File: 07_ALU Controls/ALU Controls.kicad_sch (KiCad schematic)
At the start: 7 parts, among them J1 Operators 1, J2 Operators 2, J3 Operand, J4 Data Bus, J5 Alu-Out Bus, J6 Input 1, J7 Input 2

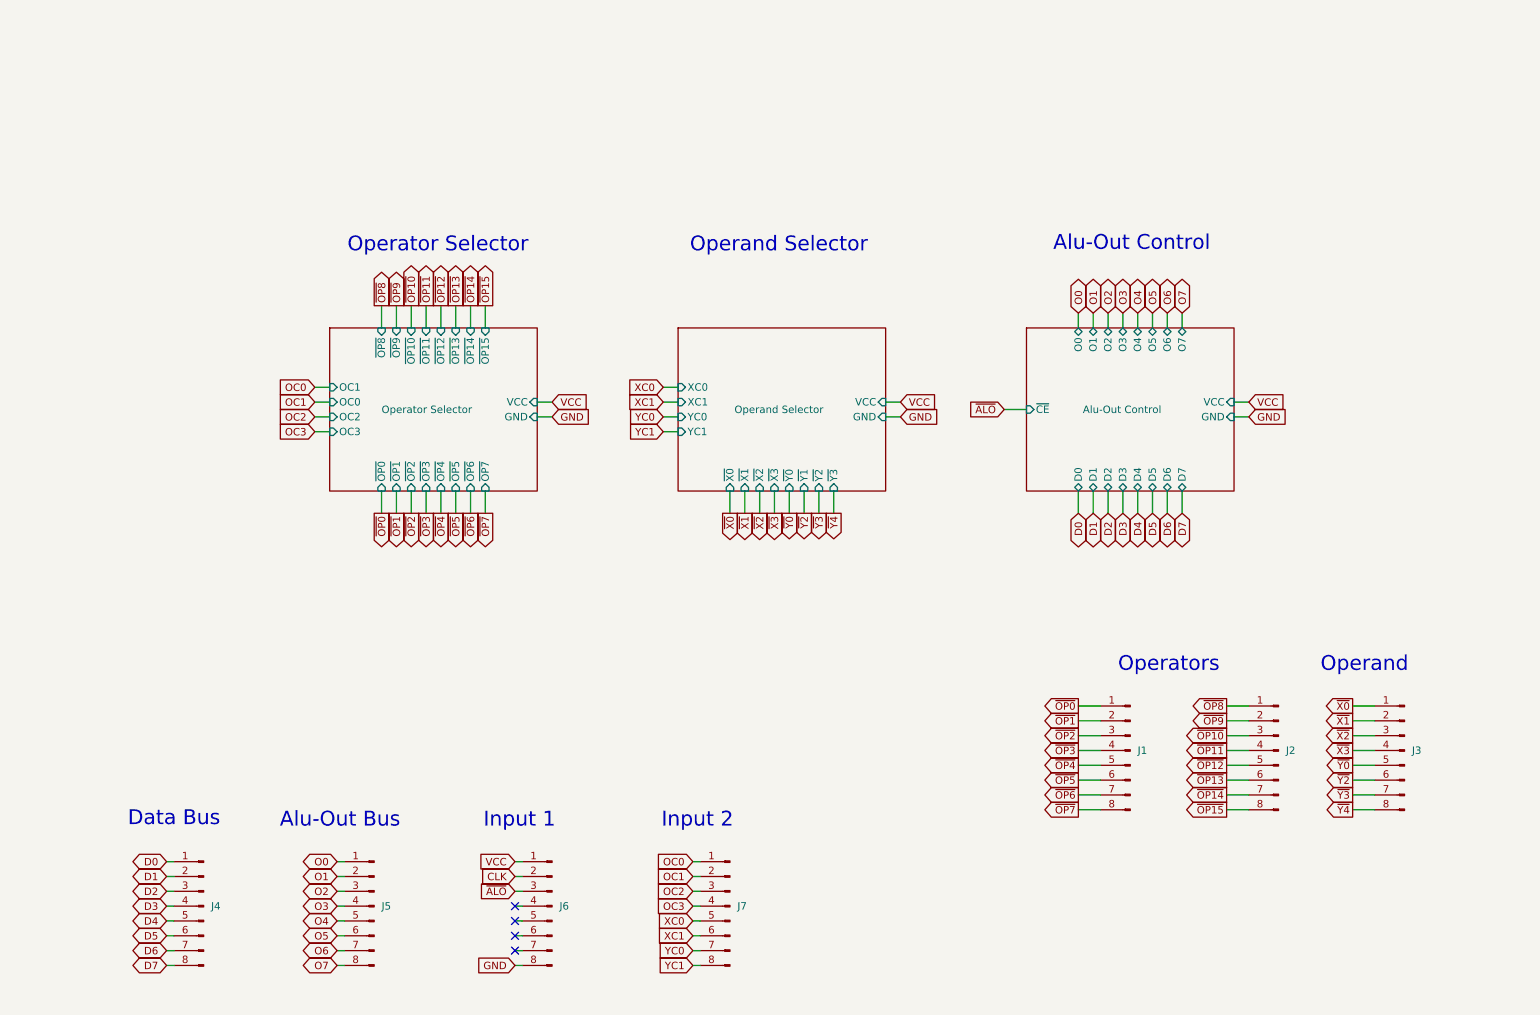
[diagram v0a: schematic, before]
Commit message: Last revision of the cpu, all boards have been ordered. Implementation to be tested and documented in following commits.
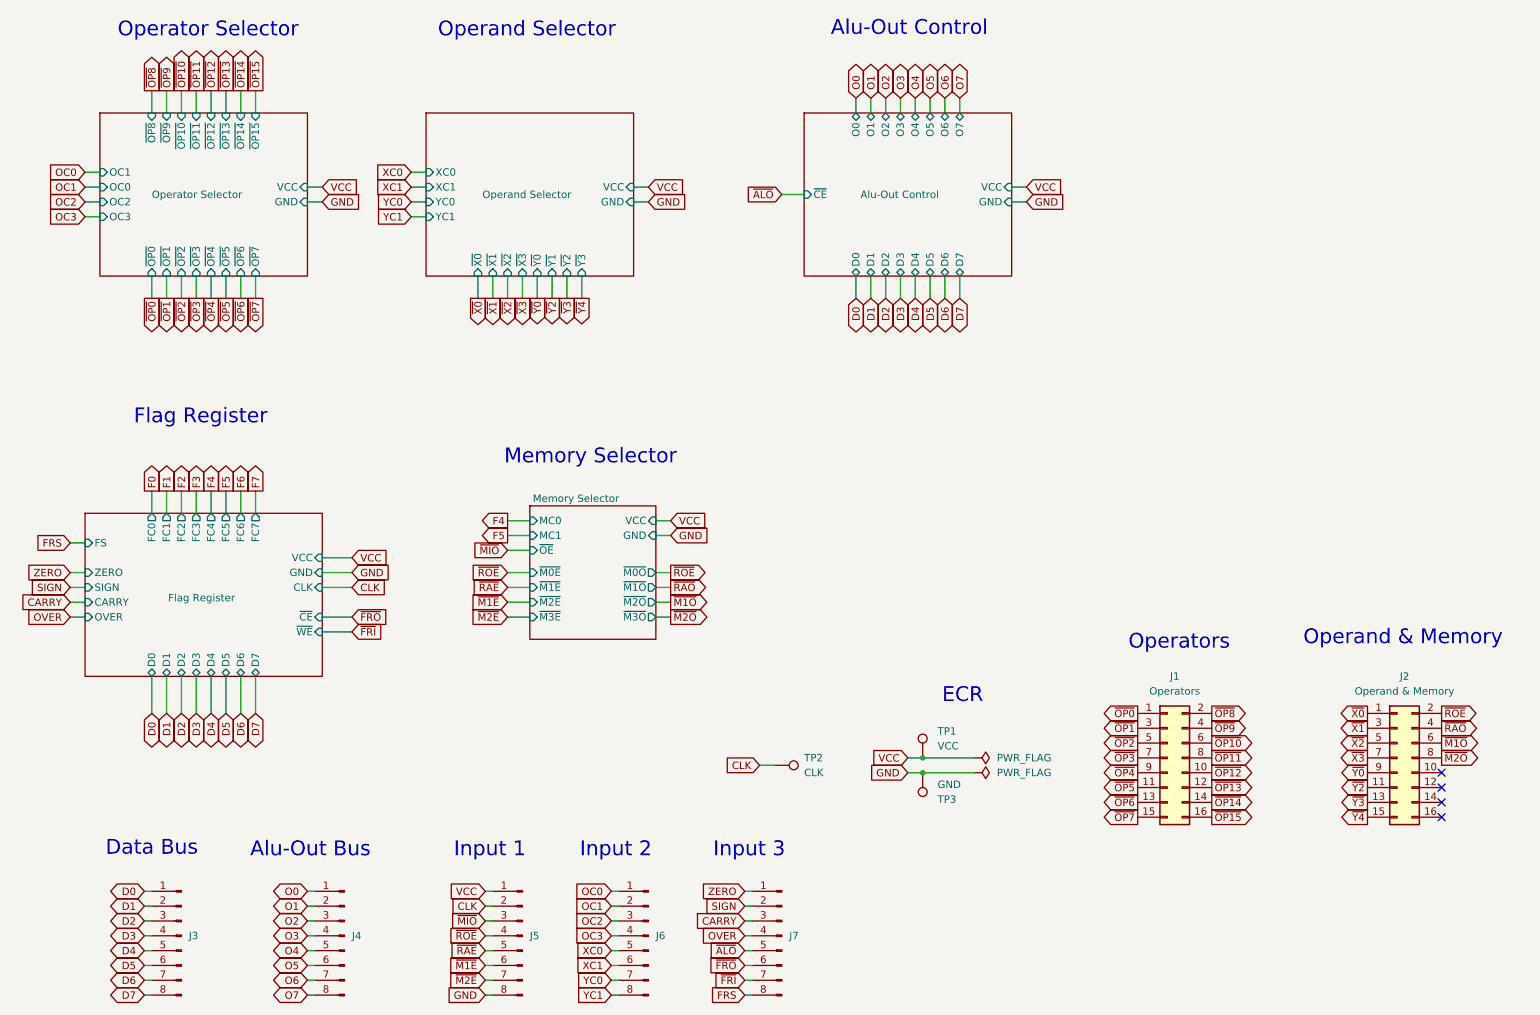
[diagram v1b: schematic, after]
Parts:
- removed J1: Operators 1, Custom:PinHeader_1x08_P2.54mm_Vertical, symbol Connector:Conn_01x08_Pin
- removed J2: Operators 2, Custom:PinHeader_1x08_P2.54mm_Vertical, symbol Connector:Conn_01x08_Pin
- removed J3: Operand, Custom:PinHeader_1x08_P2.54mm_Vertical, symbol Connector:Conn_01x08_Pin
- added J1: Operators, Connector_PinHeader_2.54mm:PinHeader_2x08_P2.54mm_Horizontal, symbol Connector_Generic:Conn_02x08_Odd_Even
- added J2: Operand & Memory, Connector_PinHeader_2.54mm:PinHeader_2x08_P2.54mm_Horizontal, symbol Connector_Generic:Conn_02x08_Odd_Even
- added J7: Input 3, Custom:PinHeader_1x08_P2.54mm_Horizontal, symbol Connector:Conn_01x08_Pin
- added TP1: VCC, TestPoint:TestPoint_Loop_D3.50mm_Drill0.9mm_Beaded, symbol Connector:TestPoint
- added TP2: CLK, TestPoint:TestPoint_Loop_D3.50mm_Drill0.9mm_Beaded, symbol Connector:TestPoint
- added TP3: GND, TestPoint:TestPoint_Loop_D3.50mm_Drill0.9mm_Beaded, symbol Connector:TestPoint
- renumbered J4 to J3, J5 to J4, J6 to J5, J7 to J6
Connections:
- net CLK: now also TP2.1
- net GND: now also TP3.1
- net VCC: now also TP1.1
- net ~{ALO}: now also J7.5 (Pin_5); no longer J5.3 (Pin_3)
- net ~{OP0}: now also J1.1 (Pin_1)
- net ~{OP10}: now also J1.6 (Pin_6)
- net ~{OP11}: now also J1.8 (Pin_8)
- net ~{OP12}: now also J1.10 (Pin_10)
- net ~{OP13}: now also J1.12 (Pin_12)
- net ~{OP14}: now also J1.14 (Pin_14)
- net ~{OP15}: now also J1.16 (Pin_16)
- net ~{OP1}: now also J1.3 (Pin_3)
- net ~{OP2}: now also J1.5 (Pin_5)
- net ~{OP3}: now also J1.7 (Pin_7)
- net ~{OP4}: now also J1.9 (Pin_9)
- net ~{OP5}: now also J1.11 (Pin_11)
- net ~{OP6}: now also J1.13 (Pin_13)
- net ~{OP7}: now also J1.15 (Pin_15)
- net ~{OP8}: now also J1.2 (Pin_2)
- net ~{OP9}: now also J1.4 (Pin_4)
- net ~{X0}: now also J2.1 (Pin_1)
- net ~{X1}: now also J2.3 (Pin_3)
- net ~{X2}: now also J2.5 (Pin_5)
- net ~{X3}: now also J2.7 (Pin_7)
- net ~{Y0}: now also J2.9 (Pin_9)
- net ~{Y2}: now also J2.11 (Pin_11)
- net ~{Y3}: now also J2.13 (Pin_13)
- net ~{Y4}: now also J2.15 (Pin_15)
- net ~{ROE}: now reaches J5.4 (Pin_4)
- net ~{ROE}: now also J2.2 (Pin_2)
- net ~{RAE}: now reaches J5.5 (Pin_5)
- net ~{M1E}: now reaches J5.6 (Pin_6)
- net ~{M2E}: now reaches J5.7 (Pin_7)
- new net CARRY: J7.3 (Pin_3)
- new net FRS: J7.8 (Pin_8)
- new net OVER: J7.4 (Pin_4)
- new net SIGN: J7.2 (Pin_2)
- new net ZERO: J7.1 (Pin_1)
- new net ~{FRI}: J7.7 (Pin_7)
- new net ~{FRO}: J7.6 (Pin_6)
- new net ~{M1O}: J2.6 (Pin_6)
- new net ~{M2O}: J2.8 (Pin_8)
- new net ~{MIO}: J5.3 (Pin_3)
- new net ~{RAO}: J2.4 (Pin_4)
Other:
- added sheet Flag Register (flag-register.kicad_sch)
- added sheet Memory Selector (memory-selector.kicad_sch)
- note added: "ECR"
- note added: "Flag Register"
- note added: "Input 3"
- note added: "Memory Selector"
- note added: "Operand & Memory"
- note removed: "Operand"
- moved on the sheet: J3, J4, J5, J6
